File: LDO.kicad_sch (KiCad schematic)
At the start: 5 parts

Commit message: CAN nano & CAN debug nano
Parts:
- gave numbers to parts that had none: 5
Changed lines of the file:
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@@
 		(dnp no)
 		(fields_autoplaced yes)
-		(property "Reference" "C?"
+		(property "Reference" "C39"
 			(at 168.275 68.5735 0)
 			(show_name no)
@@
 			(project "PS-PrechargeBoard"
 				(path "/74d17fe6-68d4-4bd7-954a-e2bbb58b1f1e/0def18ef-81e8-47ac-b719-2d9f8237a855/d07b4748-03cd-4373-ba6d-42f770522878"
-					(reference "C?")
+					(reference "C39")
 					(unit 1)
 				)
@@
 			(project "lv"
 				(path "/88356d12-c87f-4bdd-bbd8-756414c90a6d/d07b4748-03cd-4373-ba6d-42f770522878"
-					(reference "C?")
-					(unit 1)
-				)
-			)
-			(project "PS-PrechargeBoard"
-				(path "/9641192f-df6c-4894-9070-848e3256daf8/d07b4748-03cd-4373-ba6d-42f770522878"
 					(reference "C?")
 					(unit 1)
@@
 		(in_pos_files yes)
 		(dnp no)
-		(property "Reference" "TP_3.3V?"
+		(property "Reference" "TP_3.3V1"
 			(at 166.624 54.356 90)
 			(show_name no)
@@
 			(project "PS-PrechargeBoard"
 				(path "/74d17fe6-68d4-4bd7-954a-e2bbb58b1f1e/0def18ef-81e8-47ac-b719-2d9f8237a855/d07b4748-03cd-4373-ba6d-42f770522878"
-					(reference "TP_3.3V?")
+					(reference "TP_3.3V1")
 					(unit 1)
 				)
@@
 			(project "lv"
 				(path "/88356d12-c87f-4bdd-bbd8-756414c90a6d/d07b4748-03cd-4373-ba6d-42f770522878"
-					(reference "TP_3.3V?")
-					(unit 1)
-				)
-			)
-			(project "PS-PrechargeBoard"
-				(path "/9641192f-df6c-4894-9070-848e3256daf8/d07b4748-03cd-4373-ba6d-42f770522878"
 					(reference "TP_3.3V?")
 					(unit 1)
@@
 		(dnp no)
 		(fields_autoplaced yes)
-		(property "Reference" "U?"
+		(property "Reference" "U4"
 			(at 152.4 56.515 0)
 			(show_name no)
@@
 			(project "PS-PrechargeBoard"
 				(path "/74d17fe6-68d4-4bd7-954a-e2bbb58b1f1e/0def18ef-81e8-47ac-b719-2d9f8237a855/d07b4748-03cd-4373-ba6d-42f770522878"
-					(reference "U?")
+					(reference "U4")
 					(unit 1)
 				)
@@
 			(project "lv"
 				(path "/88356d12-c87f-4bdd-bbd8-756414c90a6d/d07b4748-03cd-4373-ba6d-42f770522878"
-					(reference "U?")
-					(unit 1)
-				)
-			)
-			(project "PS-PrechargeBoard"
-				(path "/9641192f-df6c-4894-9070-848e3256daf8/d07b4748-03cd-4373-ba6d-42f770522878"
 					(reference "U?")
 					(unit 1)
@@
 		(dnp no)
 		(fields_autoplaced yes)
-		(property "Reference" "D?"
+		(property "Reference" "D9"
 			(at 133.604 57.15 0)
 			(show_name no)
@@
 			(project "PS-PrechargeBoard"
 				(path "/74d17fe6-68d4-4bd7-954a-e2bbb58b1f1e/0def18ef-81e8-47ac-b719-2d9f8237a855/d07b4748-03cd-4373-ba6d-42f770522878"
-					(reference "D?")
+					(reference "D9")
 					(unit 1)
 				)
@@
 			(project "lv"
 				(path "/88356d12-c87f-4bdd-bbd8-756414c90a6d/d07b4748-03cd-4373-ba6d-42f770522878"
-					(reference "D?")
-					(unit 1)
-				)
-			)
-			(project "PS-PrechargeBoard"
-				(path "/9641192f-df6c-4894-9070-848e3256daf8/d07b4748-03cd-4373-ba6d-42f770522878"
 					(reference "D?")
 					(unit 1)
@@
 		(dnp no)
 		(fields_autoplaced yes)
-		(property "Reference" "C?"
+		(property "Reference" "C38"
 			(at 142.875 68.5735 0)
 			(show_name no)
@@
 			(project "PS-PrechargeBoard"
 				(path "/74d17fe6-68d4-4bd7-954a-e2bbb58b1f1e/0def18ef-81e8-47ac-b719-2d9f8237a855/d07b4748-03cd-4373-ba6d-42f770522878"
-					(reference "C?")
+					(reference "C38")
 					(unit 1)
 				)
@@
 					(reference "C?")
 					(unit 1)
-				)
-			)
-			(project "PS-PrechargeBoard"
-				(path "/9641192f-df6c-4894-9070-848e3256daf8/d07b4748-03cd-4373-ba6d-42f770522878"
-					(reference "C?")
-					(unit 1)

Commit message: battery voltage & motor voltage
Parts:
- renumbered C38 to C26, C39 to C27, D9 to D6, U4 to U6
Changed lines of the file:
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@@
 		(dnp no)
 		(fields_autoplaced yes)
-		(property "Reference" "C39"
+		(property "Reference" "C27"
 			(at 168.275 68.5735 0)
 			(show_name no)
@@
 			(project "PS-PrechargeBoard"
 				(path "/74d17fe6-68d4-4bd7-954a-e2bbb58b1f1e/0def18ef-81e8-47ac-b719-2d9f8237a855/d07b4748-03cd-4373-ba6d-42f770522878"
-					(reference "C39")
+					(reference "C27")
 					(unit 1)
 				)
@@
 		(dnp no)
 		(fields_autoplaced yes)
-		(property "Reference" "U4"
+		(property "Reference" "U6"
 			(at 152.4 56.515 0)
 			(show_name no)
@@
 			(project "PS-PrechargeBoard"
 				(path "/74d17fe6-68d4-4bd7-954a-e2bbb58b1f1e/0def18ef-81e8-47ac-b719-2d9f8237a855/d07b4748-03cd-4373-ba6d-42f770522878"
-					(reference "U4")
+					(reference "U6")
 					(unit 1)
 				)
@@
 		(dnp no)
 		(fields_autoplaced yes)
-		(property "Reference" "D9"
+		(property "Reference" "D6"
 			(at 133.604 57.15 0)
 			(show_name no)
@@
 			(project "PS-PrechargeBoard"
 				(path "/74d17fe6-68d4-4bd7-954a-e2bbb58b1f1e/0def18ef-81e8-47ac-b719-2d9f8237a855/d07b4748-03cd-4373-ba6d-42f770522878"
-					(reference "D9")
+					(reference "D6")
 					(unit 1)
 				)
@@
 		(dnp no)
 		(fields_autoplaced yes)
-		(property "Reference" "C38"
+		(property "Reference" "C26"
 			(at 142.875 68.5735 0)
 			(show_name no)
@@
 			(project "PS-PrechargeBoard"
 				(path "/74d17fe6-68d4-4bd7-954a-e2bbb58b1f1e/0def18ef-81e8-47ac-b719-2d9f8237a855/d07b4748-03cd-4373-ba6d-42f770522878"
-					(reference "C38")
-					(unit 1)
-				)
+					(reference "C26")
+					(unit 1)
+				)

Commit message: mini review notes
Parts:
- renumbered D6 to D8
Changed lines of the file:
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@@
 		(dnp no)
 		(fields_autoplaced yes)
-		(property "Reference" "D6"
+		(property "Reference" "D8"
 			(at 133.604 57.15 0)
 			(show_name no)
@@
 			(project "PS-PrechargeBoard"
 				(path "/74d17fe6-68d4-4bd7-954a-e2bbb58b1f1e/0def18ef-81e8-47ac-b719-2d9f8237a855/d07b4748-03cd-4373-ba6d-42f770522878"
-					(reference "D6")
+					(reference "D8")
 					(unit 1)
 				)

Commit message: shifted hierarchical sheets
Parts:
- renumbered C27 to C?, C26 to C?, D8 to D?, TP_3.3V1 to TP_3.3V?, U6 to U?
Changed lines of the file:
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@@
 		(dnp no)
 		(fields_autoplaced yes)
-		(property "Reference" "C27"
+		(property "Reference" "C?"
 			(at 168.275 68.5735 0)
 			(show_name no)
@@
 		(instances
 			(project "PS-PrechargeBoard"
-				(path "/74d17fe6-68d4-4bd7-954a-e2bbb58b1f1e/0def18ef-81e8-47ac-b719-2d9f8237a855/d07b4748-03cd-4373-ba6d-42f770522878"
-					(reference "C27")
-					(unit 1)
-				)
-			)
-			(project "lv"
-				(path "/88356d12-c87f-4bdd-bbd8-756414c90a6d/d07b4748-03cd-4373-ba6d-42f770522878"
+				(path "/74d17fe6-68d4-4bd7-954a-e2bbb58b1f1e/89c84dd0-0e2d-4c17-95c7-1a7785608971"
 					(reference "C?")
 					(unit 1)
@@
 		(in_pos_files yes)
 		(dnp no)
-		(property "Reference" "TP_3.3V1"
+		(property "Reference" "TP_3.3V?"
 			(at 166.624 54.356 90)
 			(show_name no)
@@
 		(instances
 			(project "PS-PrechargeBoard"
-				(path "/74d17fe6-68d4-4bd7-954a-e2bbb58b1f1e/0def18ef-81e8-47ac-b719-2d9f8237a855/d07b4748-03cd-4373-ba6d-42f770522878"
-					(reference "TP_3.3V1")
-					(unit 1)
-				)
-			)
-			(project "lv"
-				(path "/88356d12-c87f-4bdd-bbd8-756414c90a6d/d07b4748-03cd-4373-ba6d-42f770522878"
+				(path "/74d17fe6-68d4-4bd7-954a-e2bbb58b1f1e/89c84dd0-0e2d-4c17-95c7-1a7785608971"
 					(reference "TP_3.3V?")
 					(unit 1)
@@
 		(dnp no)
 		(fields_autoplaced yes)
-		(property "Reference" "U6"
+		(property "Reference" "U?"
 			(at 152.4 56.515 0)
 			(show_name no)
@@
 		(instances
 			(project "PS-PrechargeBoard"
-				(path "/74d17fe6-68d4-4bd7-954a-e2bbb58b1f1e/0def18ef-81e8-47ac-b719-2d9f8237a855/d07b4748-03cd-4373-ba6d-42f770522878"
-					(reference "U6")
-					(unit 1)
-				)
-			)
-			(project "lv"
-				(path "/88356d12-c87f-4bdd-bbd8-756414c90a6d/d07b4748-03cd-4373-ba6d-42f770522878"
+				(path "/74d17fe6-68d4-4bd7-954a-e2bbb58b1f1e/89c84dd0-0e2d-4c17-95c7-1a7785608971"
 					(reference "U?")
 					(unit 1)
@@
 		(dnp no)
 		(fields_autoplaced yes)
-		(property "Reference" "D8"
+		(property "Reference" "D?"
 			(at 133.604 57.15 0)
 			(show_name no)
@@
 		(instances
 			(project "PS-PrechargeBoard"
-				(path "/74d17fe6-68d4-4bd7-954a-e2bbb58b1f1e/0def18ef-81e8-47ac-b719-2d9f8237a855/d07b4748-03cd-4373-ba6d-42f770522878"
-					(reference "D8")
-					(unit 1)
-				)
-			)
-			(project "lv"
-				(path "/88356d12-c87f-4bdd-bbd8-756414c90a6d/d07b4748-03cd-4373-ba6d-42f770522878"
+				(path "/74d17fe6-68d4-4bd7-954a-e2bbb58b1f1e/89c84dd0-0e2d-4c17-95c7-1a7785608971"
 					(reference "D?")
 					(unit 1)
@@
 		(dnp no)
 		(fields_autoplaced yes)
-		(property "Reference" "C26"
+		(property "Reference" "C?"
 			(at 142.875 68.5735 0)
 			(show_name no)
@@
 		(instances
 			(project "PS-PrechargeBoard"
-				(path "/74d17fe6-68d4-4bd7-954a-e2bbb58b1f1e/0def18ef-81e8-47ac-b719-2d9f8237a855/d07b4748-03cd-4373-ba6d-42f770522878"
-					(reference "C26")
-					(unit 1)
-				)
-			)
-			(project "lv"
-				(path "/88356d12-c87f-4bdd-bbd8-756414c90a6d/d07b4748-03cd-4373-ba6d-42f770522878"
+				(path "/74d17fe6-68d4-4bd7-954a-e2bbb58b1f1e/89c84dd0-0e2d-4c17-95c7-1a7785608971"
 					(reference "C?")
 					(unit 1)

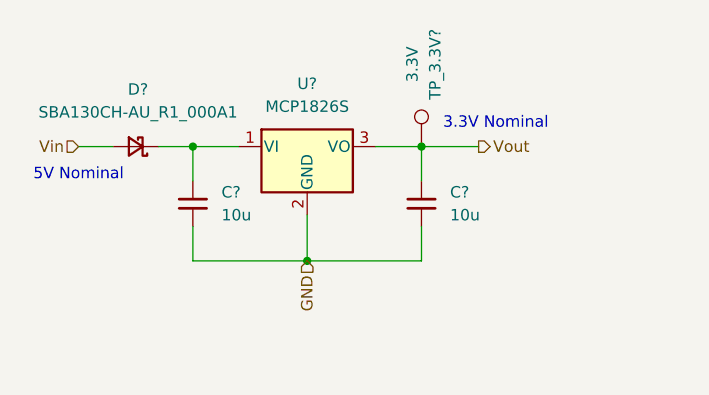
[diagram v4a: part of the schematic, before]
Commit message: V_OUT_BAT & V_OUT_MOT & PRECHARGE_CTRL to MCU
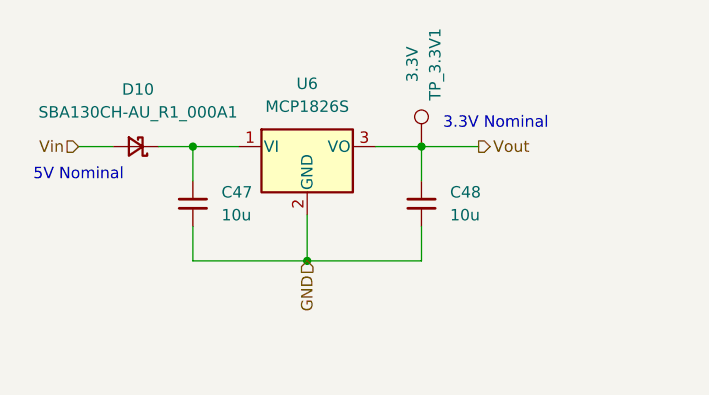
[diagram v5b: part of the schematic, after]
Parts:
- gave numbers to parts that had none: 5
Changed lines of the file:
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@@
 		(dnp no)
 		(fields_autoplaced yes)
-		(property "Reference" "C?"
+		(property "Reference" "C48"
 			(at 168.275 68.5735 0)
 			(show_name no)
@@
 			(project "PS-PrechargeBoard"
 				(path "/74d17fe6-68d4-4bd7-954a-e2bbb58b1f1e/89c84dd0-0e2d-4c17-95c7-1a7785608971"
-					(reference "C?")
+					(reference "C48")
 					(unit 1)
 				)
@@
 		(in_pos_files yes)
 		(dnp no)
-		(property "Reference" "TP_3.3V?"
+		(property "Reference" "TP_3.3V1"
 			(at 166.624 54.356 90)
 			(show_name no)
@@
 			(project "PS-PrechargeBoard"
 				(path "/74d17fe6-68d4-4bd7-954a-e2bbb58b1f1e/89c84dd0-0e2d-4c17-95c7-1a7785608971"
-					(reference "TP_3.3V?")
+					(reference "TP_3.3V1")
 					(unit 1)
 				)
@@
 		(dnp no)
 		(fields_autoplaced yes)
-		(property "Reference" "U?"
+		(property "Reference" "U6"
 			(at 152.4 56.515 0)
 			(show_name no)
@@
 			(project "PS-PrechargeBoard"
 				(path "/74d17fe6-68d4-4bd7-954a-e2bbb58b1f1e/89c84dd0-0e2d-4c17-95c7-1a7785608971"
-					(reference "U?")
+					(reference "U6")
 					(unit 1)
 				)
@@
 		(dnp no)
 		(fields_autoplaced yes)
-		(property "Reference" "D?"
+		(property "Reference" "D10"
 			(at 133.604 57.15 0)
 			(show_name no)
@@
 			(project "PS-PrechargeBoard"
 				(path "/74d17fe6-68d4-4bd7-954a-e2bbb58b1f1e/89c84dd0-0e2d-4c17-95c7-1a7785608971"
-					(reference "D?")
+					(reference "D10")
 					(unit 1)
 				)
@@
 		(dnp no)
 		(fields_autoplaced yes)
-		(property "Reference" "C?"
+		(property "Reference" "C47"
 			(at 142.875 68.5735 0)
 			(show_name no)
@@
 			(project "PS-PrechargeBoard"
 				(path "/74d17fe6-68d4-4bd7-954a-e2bbb58b1f1e/89c84dd0-0e2d-4c17-95c7-1a7785608971"
-					(reference "C?")
+					(reference "C47")
 					(unit 1)
 				)

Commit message: precharges & voltage sensors
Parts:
- renumbered C47 to C28, C48 to C29, D10 to D2
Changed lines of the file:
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@@
 		(dnp no)
 		(fields_autoplaced yes)
-		(property "Reference" "C48"
+		(property "Reference" "C29"
 			(at 168.275 68.5735 0)
 			(show_name no)
@@
 		(instances
 			(project "PS-PrechargeBoard"
-				(path "/74d17fe6-68d4-4bd7-954a-e2bbb58b1f1e/89c84dd0-0e2d-4c17-95c7-1a7785608971"
-					(reference "C48")
+				(path "/74d17fe6-68d4-4bd7-954a-e2bbb58b1f1e/c6e51092-efec-40a8-afae-63cae62691f2/90ec3f79-b3d6-4fd7-840b-31d3af1f4c2b"
+					(reference "C29")
 					(unit 1)
 				)
@@
 		(instances
 			(project "PS-PrechargeBoard"
-				(path "/74d17fe6-68d4-4bd7-954a-e2bbb58b1f1e/89c84dd0-0e2d-4c17-95c7-1a7785608971"
+				(path "/74d17fe6-68d4-4bd7-954a-e2bbb58b1f1e/c6e51092-efec-40a8-afae-63cae62691f2/90ec3f79-b3d6-4fd7-840b-31d3af1f4c2b"
 					(reference "TP_3.3V1")
 					(unit 1)
@@
 		(instances
 			(project "PS-PrechargeBoard"
-				(path "/74d17fe6-68d4-4bd7-954a-e2bbb58b1f1e/89c84dd0-0e2d-4c17-95c7-1a7785608971"
+				(path "/74d17fe6-68d4-4bd7-954a-e2bbb58b1f1e/c6e51092-efec-40a8-afae-63cae62691f2/90ec3f79-b3d6-4fd7-840b-31d3af1f4c2b"
 					(reference "U6")
 					(unit 1)
@@
 		(dnp no)
 		(fields_autoplaced yes)
-		(property "Reference" "D10"
+		(property "Reference" "D2"
 			(at 133.604 57.15 0)
 			(show_name no)
@@
 		(instances
 			(project "PS-PrechargeBoard"
-				(path "/74d17fe6-68d4-4bd7-954a-e2bbb58b1f1e/89c84dd0-0e2d-4c17-95c7-1a7785608971"
-					(reference "D10")
+				(path "/74d17fe6-68d4-4bd7-954a-e2bbb58b1f1e/c6e51092-efec-40a8-afae-63cae62691f2/90ec3f79-b3d6-4fd7-840b-31d3af1f4c2b"
+					(reference "D2")
 					(unit 1)
 				)
@@
 		(dnp no)
 		(fields_autoplaced yes)
-		(property "Reference" "C47"
+		(property "Reference" "C28"
 			(at 142.875 68.5735 0)
 			(show_name no)
@@
 		(instances
 			(project "PS-PrechargeBoard"
-				(path "/74d17fe6-68d4-4bd7-954a-e2bbb58b1f1e/89c84dd0-0e2d-4c17-95c7-1a7785608971"
-					(reference "C47")
+				(path "/74d17fe6-68d4-4bd7-954a-e2bbb58b1f1e/c6e51092-efec-40a8-afae-63cae62691f2/90ec3f79-b3d6-4fd7-840b-31d3af1f4c2b"
+					(reference "C28")
 					(unit 1)
 				)

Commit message: saving
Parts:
- renumbered C29 to C?, C28 to C?, D2 to D?, TP_3.3V1 to TP_3.3V?, U6 to U?
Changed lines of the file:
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@@
 		(dnp no)
 		(fields_autoplaced yes)
-		(property "Reference" "C29"
+		(property "Reference" "C?"
 			(at 168.275 68.5735 0)
 			(show_name no)
@@
 		(instances
 			(project "PS-PrechargeBoard"
-				(path "/74d17fe6-68d4-4bd7-954a-e2bbb58b1f1e/c6e51092-efec-40a8-afae-63cae62691f2/90ec3f79-b3d6-4fd7-840b-31d3af1f4c2b"
-					(reference "C29")
+				(path "/74d17fe6-68d4-4bd7-954a-e2bbb58b1f1e/3009d091-62bc-471a-b662-9169ff7ac007"
+					(reference "C?")
 					(unit 1)
 				)
@@
 		(in_pos_files yes)
 		(dnp no)
-		(property "Reference" "TP_3.3V1"
+		(property "Reference" "TP_3.3V?"
 			(at 166.624 54.356 90)
 			(show_name no)
@@
 		(instances
 			(project "PS-PrechargeBoard"
-				(path "/74d17fe6-68d4-4bd7-954a-e2bbb58b1f1e/c6e51092-efec-40a8-afae-63cae62691f2/90ec3f79-b3d6-4fd7-840b-31d3af1f4c2b"
-					(reference "TP_3.3V1")
+				(path "/74d17fe6-68d4-4bd7-954a-e2bbb58b1f1e/3009d091-62bc-471a-b662-9169ff7ac007"
+					(reference "TP_3.3V?")
 					(unit 1)
 				)
@@
 		(dnp no)
 		(fields_autoplaced yes)
-		(property "Reference" "U6"
+		(property "Reference" "U?"
 			(at 152.4 56.515 0)
 			(show_name no)
@@
 		(instances
 			(project "PS-PrechargeBoard"
-				(path "/74d17fe6-68d4-4bd7-954a-e2bbb58b1f1e/c6e51092-efec-40a8-afae-63cae62691f2/90ec3f79-b3d6-4fd7-840b-31d3af1f4c2b"
-					(reference "U6")
+				(path "/74d17fe6-68d4-4bd7-954a-e2bbb58b1f1e/3009d091-62bc-471a-b662-9169ff7ac007"
+					(reference "U?")
 					(unit 1)
 				)
@@
 		(dnp no)
 		(fields_autoplaced yes)
-		(property "Reference" "D2"
+		(property "Reference" "D?"
 			(at 133.604 57.15 0)
 			(show_name no)
@@
 		(instances
 			(project "PS-PrechargeBoard"
-				(path "/74d17fe6-68d4-4bd7-954a-e2bbb58b1f1e/c6e51092-efec-40a8-afae-63cae62691f2/90ec3f79-b3d6-4fd7-840b-31d3af1f4c2b"
-					(reference "D2")
+				(path "/74d17fe6-68d4-4bd7-954a-e2bbb58b1f1e/3009d091-62bc-471a-b662-9169ff7ac007"
+					(reference "D?")
 					(unit 1)
 				)
@@
 		(dnp no)
 		(fields_autoplaced yes)
-		(property "Reference" "C28"
+		(property "Reference" "C?"
 			(at 142.875 68.5735 0)
 			(show_name no)
@@
 		(instances
 			(project "PS-PrechargeBoard"
-				(path "/74d17fe6-68d4-4bd7-954a-e2bbb58b1f1e/c6e51092-efec-40a8-afae-63cae62691f2/90ec3f79-b3d6-4fd7-840b-31d3af1f4c2b"
-					(reference "C28")
+				(path "/74d17fe6-68d4-4bd7-954a-e2bbb58b1f1e/3009d091-62bc-471a-b662-9169ff7ac007"
+					(reference "C?")
 					(unit 1)
 				)

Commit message: final schematic REV-A?
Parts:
- gave numbers to parts that had none: 5
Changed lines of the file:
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@@
 		(dnp no)
 		(fields_autoplaced yes)
-		(property "Reference" "C?"
+		(property "Reference" "C38"
 			(at 168.275 68.5735 0)
 			(show_name no)
@@
 		(instances
 			(project "PS-PrechargeBoard"
-				(path "/74d17fe6-68d4-4bd7-954a-e2bbb58b1f1e/3009d091-62bc-471a-b662-9169ff7ac007"
-					(reference "C?")
+				(path "/74d17fe6-68d4-4bd7-954a-e2bbb58b1f1e/2ca150cf-fbe5-4d5b-a7dc-f2dc5c6024d0/948d6922-1fd9-4543-b1e5-414190ab0379"
+					(reference "C38")
 					(unit 1)
 				)
@@
 		(in_pos_files yes)
 		(dnp no)
-		(property "Reference" "TP_3.3V?"
+		(property "Reference" "TP_3.3V1"
 			(at 166.624 54.356 90)
 			(show_name no)
@@
 		(instances
 			(project "PS-PrechargeBoard"
-				(path "/74d17fe6-68d4-4bd7-954a-e2bbb58b1f1e/3009d091-62bc-471a-b662-9169ff7ac007"
-					(reference "TP_3.3V?")
+				(path "/74d17fe6-68d4-4bd7-954a-e2bbb58b1f1e/2ca150cf-fbe5-4d5b-a7dc-f2dc5c6024d0/948d6922-1fd9-4543-b1e5-414190ab0379"
+					(reference "TP_3.3V1")
 					(unit 1)
 				)
@@
 		(dnp no)
 		(fields_autoplaced yes)
-		(property "Reference" "U?"
+		(property "Reference" "U4"
 			(at 152.4 56.515 0)
 			(show_name no)
@@
 		(instances
 			(project "PS-PrechargeBoard"
-				(path "/74d17fe6-68d4-4bd7-954a-e2bbb58b1f1e/3009d091-62bc-471a-b662-9169ff7ac007"
-					(reference "U?")
+				(path "/74d17fe6-68d4-4bd7-954a-e2bbb58b1f1e/2ca150cf-fbe5-4d5b-a7dc-f2dc5c6024d0/948d6922-1fd9-4543-b1e5-414190ab0379"
+					(reference "U4")
 					(unit 1)
 				)
@@
 		(dnp no)
 		(fields_autoplaced yes)
-		(property "Reference" "D?"
+		(property "Reference" "D10"
 			(at 133.604 57.15 0)
 			(show_name no)
@@
 		(instances
 			(project "PS-PrechargeBoard"
-				(path "/74d17fe6-68d4-4bd7-954a-e2bbb58b1f1e/3009d091-62bc-471a-b662-9169ff7ac007"
-					(reference "D?")
+				(path "/74d17fe6-68d4-4bd7-954a-e2bbb58b1f1e/2ca150cf-fbe5-4d5b-a7dc-f2dc5c6024d0/948d6922-1fd9-4543-b1e5-414190ab0379"
+					(reference "D10")
 					(unit 1)
 				)
@@
 		(dnp no)
 		(fields_autoplaced yes)
-		(property "Reference" "C?"
+		(property "Reference" "C37"
 			(at 142.875 68.5735 0)
 			(show_name no)
@@
 		(instances
 			(project "PS-PrechargeBoard"
-				(path "/74d17fe6-68d4-4bd7-954a-e2bbb58b1f1e/3009d091-62bc-471a-b662-9169ff7ac007"
-					(reference "C?")
+				(path "/74d17fe6-68d4-4bd7-954a-e2bbb58b1f1e/2ca150cf-fbe5-4d5b-a7dc-f2dc5c6024d0/948d6922-1fd9-4543-b1e5-414190ab0379"
+					(reference "C37")
 					(unit 1)
 				)
